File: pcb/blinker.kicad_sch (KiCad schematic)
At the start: 9 parts, among them J1 ISP, U1 ATtiny10-TS

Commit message: Making progress
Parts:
- removed D3: LED, LED_SMD:LED_0603_1608Metric, symbol Device:LED
- removed R1: 220, Resistor_SMD:R_0603_1608Metric, symbol Device:R
- added D10, D11, D12, D13, D2, D3, D4, D5, D6, D7, D8, D9: WS2812B, LED_SMD:LED_Wurth_150044M155260, symbol LED:WS2812B
- added JP2: Jumper_2_Open, Jumper:SolderJumper-2_P1.3mm_Open_TrianglePad1.0x1.5mm, symbol Jumper:Jumper_2_Open
- added U2: M24C01-FDW, Package_SO:TSSOP-8_4.4x3mm_P0.65mm, symbol Memory_EEPROM:M24C01-FDW
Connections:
- net 2.7VCC: now also D10.1 (VDD), D11.1 (VDD), D12.1 (VDD), D13.1 (VDD)
- net 5VCC: now also JP2.2 (B), U2.8 (VCC)
- net GND: now also D2.3 (VSS), D3.3 (VSS), D4.3 (VSS), D5.3 (VSS), U2.1 (E0), U2.2 (E1), U2.3 (E2), U2.4 (VSS)
- net LED renamed LEDSTRING
- net LEDSTRING: now also D2.4 (DIN)
- net TPICLK renamed ROMSCL
- net ROMSCL: now also U2.6 (SCL)
- net TPIDATA renamed ROMSDA
- net ROMSDA: now also U2.5 (SDA)
- new net: D6.1 (VDD), D7.1 (VDD), D8.1 (VDD), D9.1 (VDD)
- new net: D10.4 (DIN), D9.2 (DOUT)
- new net: D6.3 (VSS), D7.3 (VSS), D8.3 (VSS), D9.3 (VSS)
- new net: D8.2 (DOUT), D9.4 (DIN)
- new net: D12.2 (DOUT), D13.4 (DIN)
- new net: D10.3 (VSS), D11.3 (VSS), D12.3 (VSS), D13.3 (VSS)
- new net: D11.2 (DOUT), D12.4 (DIN)
- new net: JP2.1 (A), U2.7 (~{WC})
- new net: D2.1 (VDD), D3.1 (VDD), D4.1 (VDD), D5.1 (VDD)
- new net: D5.2 (DOUT), D6.4 (DIN)
- new net: D4.2 (DOUT), D5.4 (DIN)
- new net: D2.2 (DOUT), D3.4 (DIN)
- new net: D10.2 (DOUT), D11.4 (DIN)
- new net: D7.2 (DOUT), D8.4 (DIN)
- new net: D6.2 (DOUT), D7.4 (DIN)
- new net: D3.2 (DOUT), D4.4 (DIN)

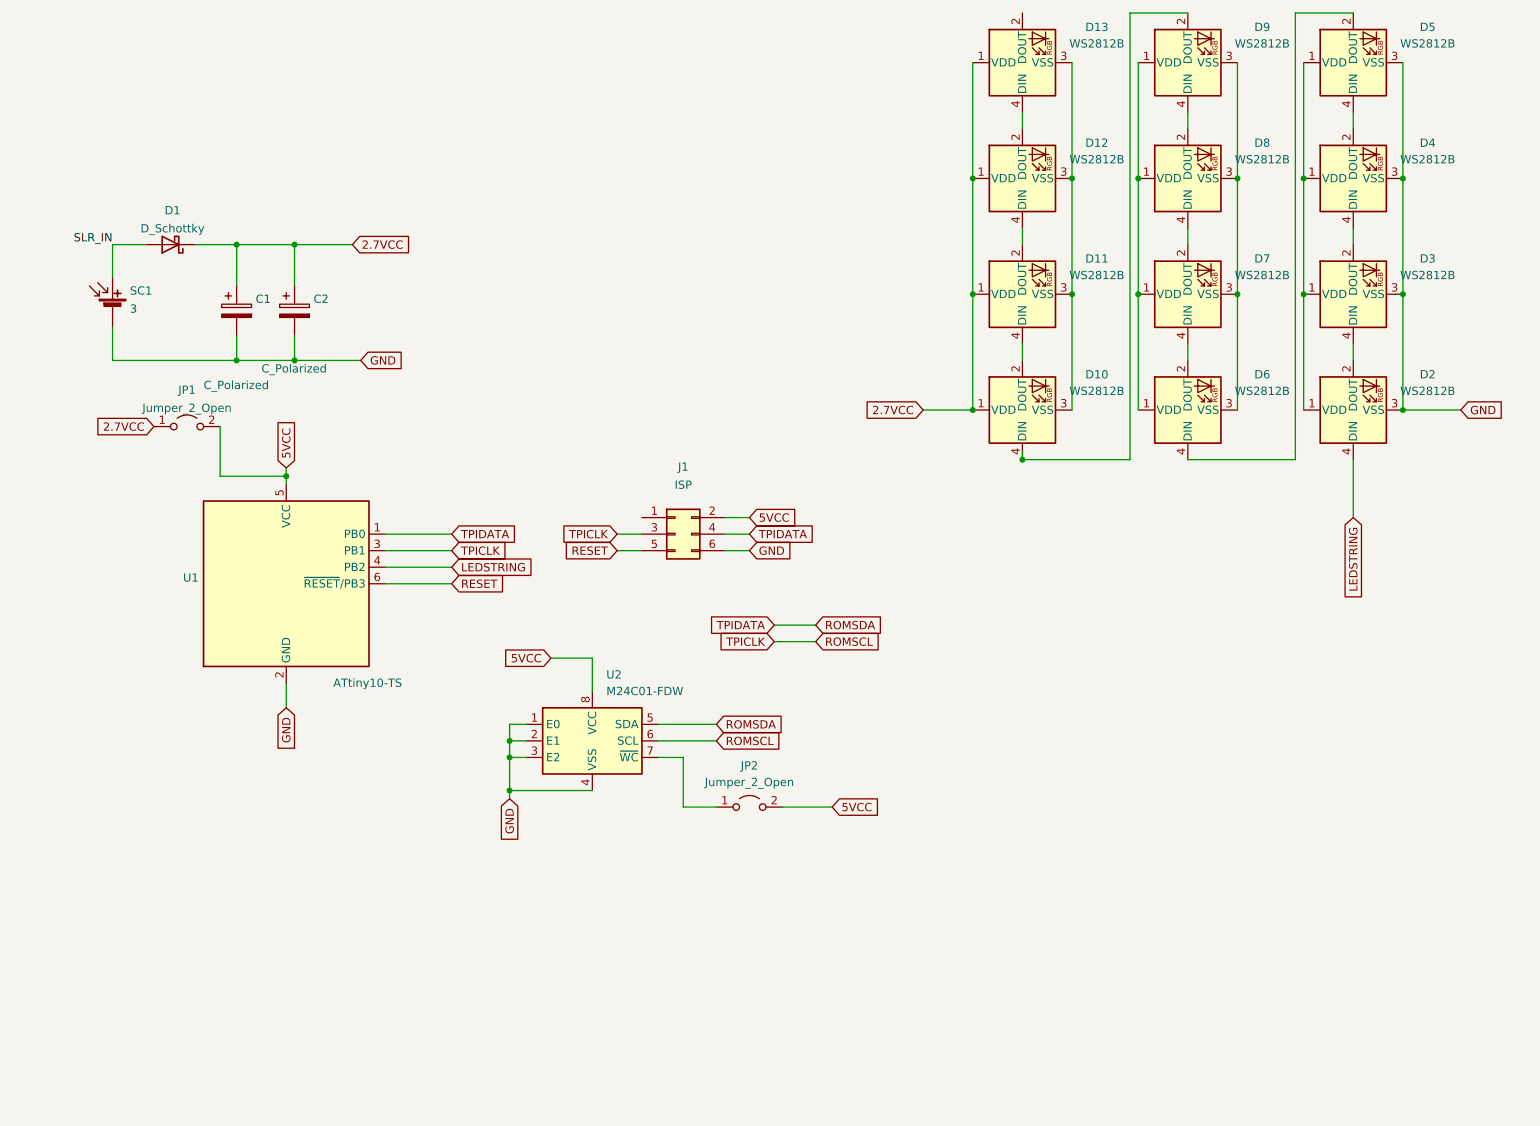
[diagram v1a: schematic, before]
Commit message: Adding decoupling caps and RC filter.
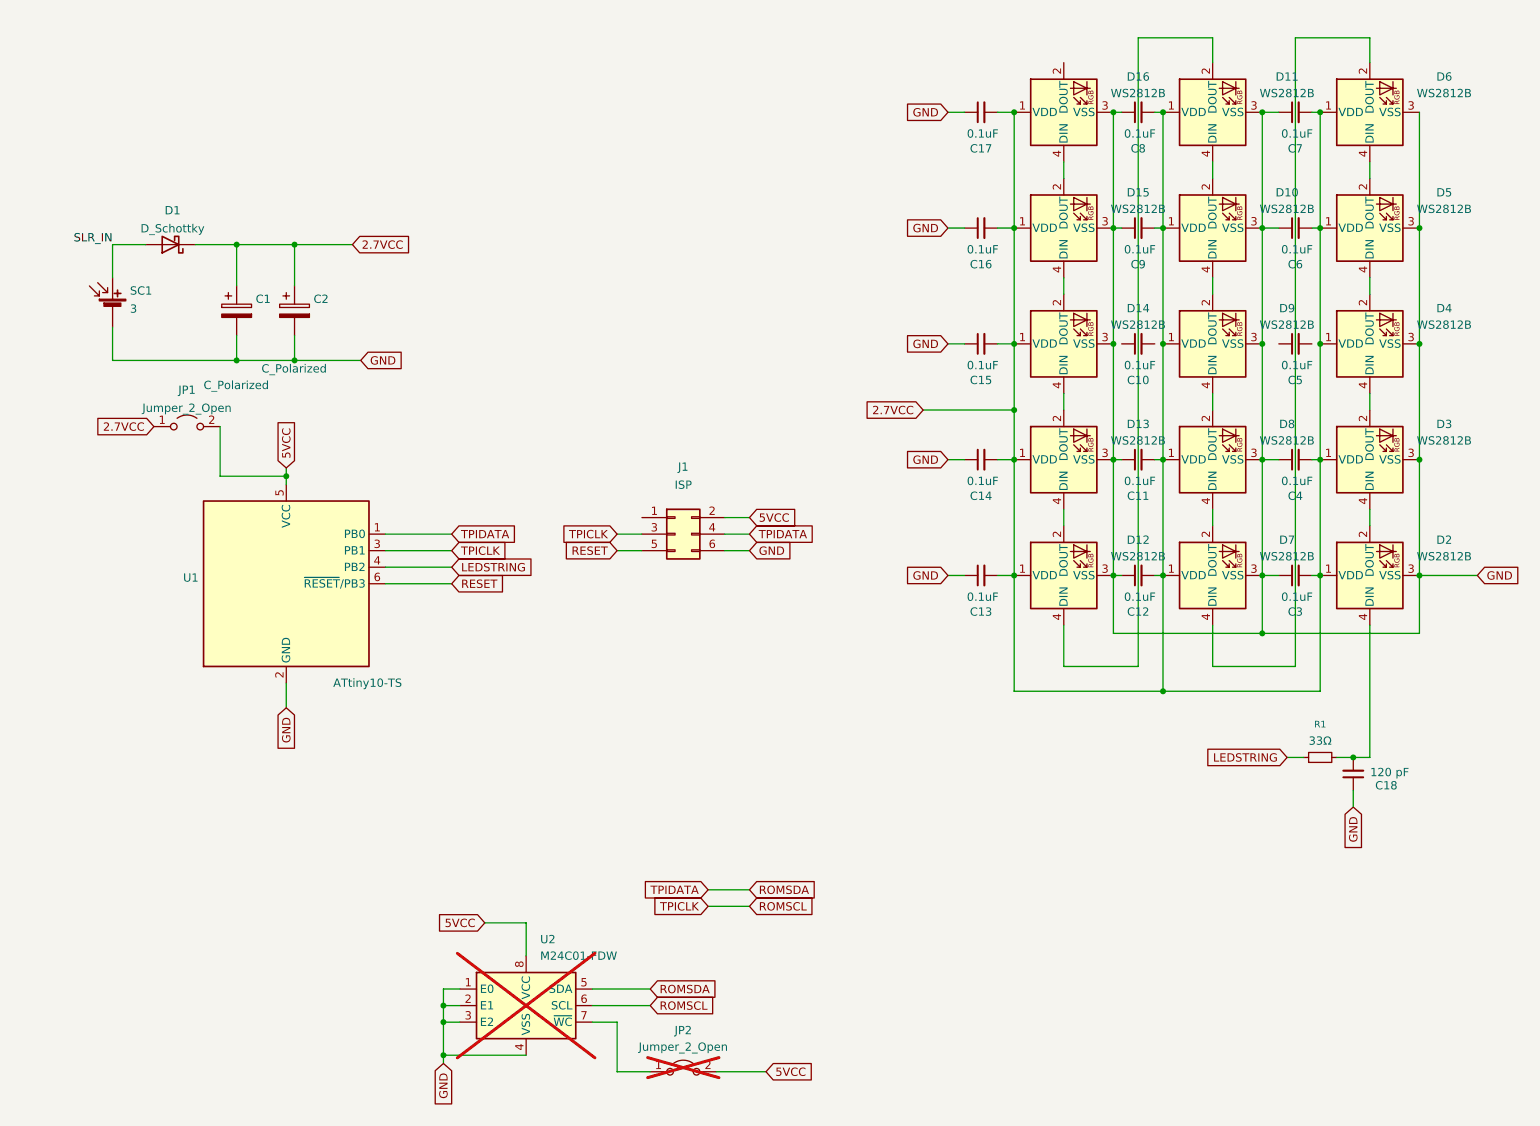
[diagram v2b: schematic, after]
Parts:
- added C10, C11, C12, C13, C14, C15, C16, C17, C3, C4, C5, C6, C7, C8, C9: 0.1uF, Capacitor_SMD:C_01005_0402Metric, symbol Device:C_Small
- added C18: 120 pF, Capacitor_SMD:C_01005_0402Metric, symbol Device:C_Small
- added D14, D15, D16: WS2812B, LED_SMD:LED_Wurth_150044M155260, symbol LED:WS2812B
- added R1: 33Ω, Resistor_SMD:R_0603_1608Metric, symbol Device:R_Small
- JP2, U2: now not fitted; now left out of the parts list
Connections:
- net 2.7VCC: now also D2.1 (VDD), D3.1 (VDD), D4.1 (VDD), D5.1 (VDD), D6.1 (VDD), D7.1 (VDD), D8.1 (VDD), D9.1 (VDD), C11.2, C12.2, C13.2, C14.2, C15.2, C16.2, C17.2, C3.2, C4.2, C6.2, C7.2, C8.2, C9.2, D14.1 (VDD), D15.1 (VDD), D16.1 (VDD)
- net GND: now also D10.3 (VSS), D11.3 (VSS), D12.3 (VSS), D13.3 (VSS), D6.3 (VSS), D7.3 (VSS), D8.3 (VSS), D9.3 (VSS), C11.1, C12.1, C13.1, C14.1, C15.1, C16.1, C17.1, C18.1, C3.1, C4.1, C6.1, C7.1, C8.1, C9.1, D14.3 (VSS), D15.3 (VSS), D16.3 (VSS)
- net LEDSTRING: now also R1.1; no longer D2.4 (DIN)
- net at D13.2 (DOUT): now also D14.4 (DIN)
- new net: D15.2 (DOUT), D16.4 (DIN)
- new net: D14.2 (DOUT), D15.4 (DIN)
- new net: C18.2, D2.4 (DIN), R1.2
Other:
- moved on the sheet: D10, D11, D12, D13, D2, D3, D4, D5, D6, D7, D8, D9

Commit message: Nearly ready to order.
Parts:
- C1, C2, J1, JP1, SC1: now left out of the parts list
- C10, C11, C12, C13, C14, C15, C16, C17, C3, C4, C5, C6, C7, C8, C9: MPN (none) -> 0402YD104KAT2A KYOCERA AVX 0402 100 nF 16 V ±10 % Tolerance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
- C18: MPN (none) -> 04023C121KAT2A KYOCERA AVX Multilayer Ceramic Capacitors ML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
- D1: MPN (none) -> B140WS-7 Diodes Inc. Rectifier Diode, Schottky, 1 Phase, 1 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
- D10, D11, D12, D13, D14, D15, D16, D2, D3, D4, D5, D6, D7, D8, D9: MPN (none) -> LTST-E133CEGBK Lite-On Triple Color LED, Ultra Bright Red/u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
- R1: MPN (none) -> ERJ-PA3F33R0V Panasonic Res Thick Film 0603 33 Ohm 1% 0.25W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
- U1: MPN (none) -> ATTINY10-TSHR Mcu 8-BIT Microchip AVR Risc 1KB Flash 2.5V/3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
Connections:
- net 2.7VCC: now also C10.2, C5.1
- net GND: now also C10.1, C5.2
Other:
- moved on the sheet: C5

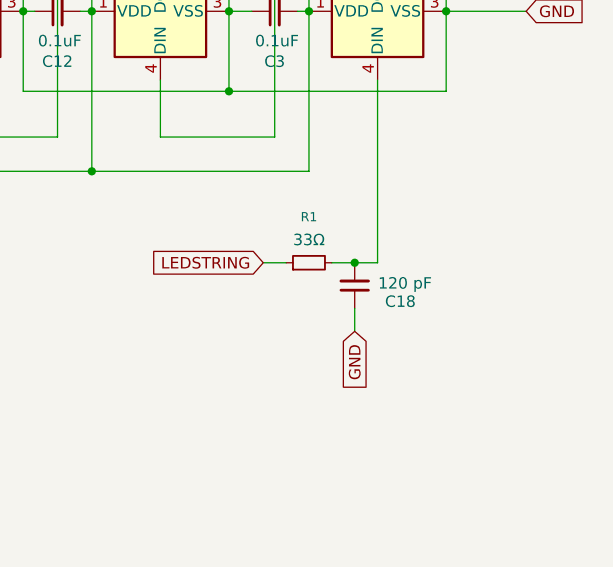
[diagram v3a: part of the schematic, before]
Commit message: Fix 0402 metric vs imperial problem.
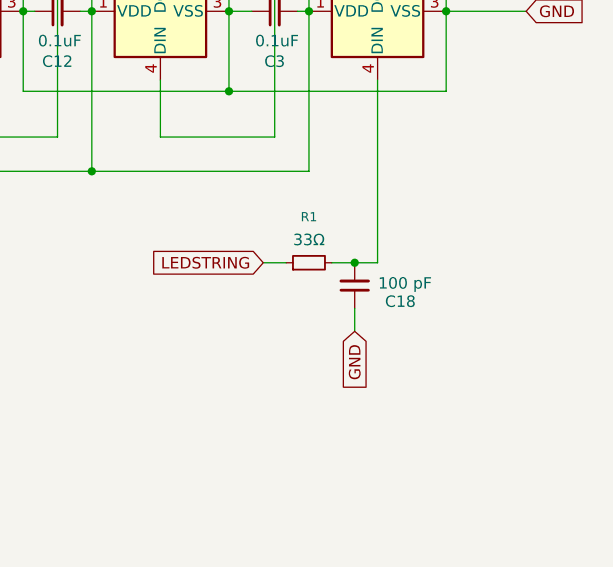
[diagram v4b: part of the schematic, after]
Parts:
- C10, C11, C12, C13, C14, C15, C16, C17, C3, C4, C5, C6, C7, C8, C9: MPN 0402YD104KAT2A KYOCERA AVX 0402 100 nF 16 V ±10 % Tolerance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 -> 01016D104KAT2A KYOCERA AVX 01005 (0402Metric) CERAMIC CAPAC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
- C18: value 120 pF -> 100 pF; MPN 04023C121KAT2A KYOCERA AVX Multilayer Ceramic Capacitors ML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 -> 01016D101KAT2A KYOCERA AVX Capacitor, SMD, MultiLayer Ceram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
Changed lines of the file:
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@@
 	(paper "A4")
 	(title_block
-		(rev "2.0")
+		(rev "2.01")
 	)
 	(junction
@@
 			)
 		)
-		(property "MPN" "0402YD104KAT2A KYOCERA AVX 0402 100 nF 16 V ±10 % Tolerance X5R Surface Mount Multilayer Ceramic Capacitor "
+		(property "MPN" "01016D104KAT2A KYOCERA AVX 01005 (0402Metric) CERAMIC CAPACITOR ceramic capacitor 6.3V 0.1muF ±10% X5R"
 			(at 245.11 95.25 90)
 			(effects
@@
 			)
 		)
-		(property "MPN" "0402YD104KAT2A KYOCERA AVX 0402 100 nF 16 V ±10 % Tolerance X5R Surface Mount Multilayer Ceramic Capacitor "
+		(property "MPN" "01016D104KAT2A KYOCERA AVX 01005 (0402Metric) CERAMIC CAPACITOR ceramic capacitor 6.3V 0.1muF ±10% X5R"
 			(at 220.98 113.03 90)
 			(effects
@@
 			)
 		)
-		(property "MPN" "0402YD104KAT2A KYOCERA AVX 0402 100 nF 16 V ±10 % Tolerance X5R Surface Mount Multilayer Ceramic Capacitor "
+		(property "MPN" "01016D104KAT2A KYOCERA AVX 01005 (0402Metric) CERAMIC CAPACITOR ceramic capacitor 6.3V 0.1muF ±10% X5R"
 			(at 245.11 77.47 90)
 			(effects
@@
 			)
 		)
-		(property "MPN" "0402YD104KAT2A KYOCERA AVX 0402 100 nF 16 V ±10 % Tolerance X5R Surface Mount Multilayer Ceramic Capacitor "
+		(property "MPN" "01016D104KAT2A KYOCERA AVX 01005 (0402Metric) CERAMIC CAPACITOR ceramic capacitor 6.3V 0.1muF ±10% X5R"
 			(at 196.85 41.91 90)
 			(effects
@@
 			)
 		)
-		(property "MPN" "0402YD104KAT2A KYOCERA AVX 0402 100 nF 16 V ±10 % Tolerance X5R Surface Mount Multilayer Ceramic Capacitor "
+		(property "MPN" "01016D104KAT2A KYOCERA AVX 01005 (0402Metric) CERAMIC CAPACITOR ceramic capacitor 6.3V 0.1muF ±10% X5R"
 			(at 220.98 77.47 90)
 			(effects
@@
 			)
 		)
-		(property "MPN" "0402YD104KAT2A KYOCERA AVX 0402 100 nF 16 V ±10 % Tolerance X5R Surface Mount Multilayer Ceramic Capacitor "
+		(property "MPN" "01016D104KAT2A KYOCERA AVX 01005 (0402Metric) CERAMIC CAPACITOR ceramic capacitor 6.3V 0.1muF ±10% X5R"
 			(at 220.98 41.91 90)
 			(effects
@@
 			)
 		)
-		(property "MPN" "0402YD104KAT2A KYOCERA AVX 0402 100 nF 16 V ±10 % Tolerance X5R Surface Mount Multilayer Ceramic Capacitor "
+		(property "MPN" "01016D104KAT2A KYOCERA AVX 01005 (0402Metric) CERAMIC CAPACITOR ceramic capacitor 6.3V 0.1muF ±10% X5R"
 			(at 220.98 95.25 90)
 			(effects
@@
 			)
 		)
-		(property "MPN" "0402YD104KAT2A KYOCERA AVX 0402 100 nF 16 V ±10 % Tolerance X5R Surface Mount Multilayer Ceramic Capacitor "
+		(property "MPN" "01016D104KAT2A KYOCERA AVX 01005 (0402Metric) CERAMIC CAPACITOR ceramic capacitor 6.3V 0.1muF ±10% X5R"
 			(at 220.98 59.69 90)
 			(effects
@@
 			)
 		)
-		(property "MPN" "0402YD104KAT2A KYOCERA AVX 0402 100 nF 16 V ±10 % Tolerance X5R Surface Mount Multilayer Ceramic Capacitor "
+		(property "MPN" "01016D104KAT2A KYOCERA AVX 01005 (0402Metric) CERAMIC CAPACITOR ceramic capacitor 6.3V 0.1muF ±10% X5R"
 			(at 245.11 59.69 90)
 			(effects
@@
 			)
 		)
-		(property "MPN" "0402YD104KAT2A KYOCERA AVX 0402 100 nF 16 V ±10 % Tolerance X5R Surface Mount Multilayer Ceramic Capacitor "
+		(property "MPN" "01016D104KAT2A KYOCERA AVX 01005 (0402Metric) CERAMIC CAPACITOR ceramic capacitor 6.3V 0.1muF ±10% X5R"
 			(at 196.85 59.69 90)
 			(effects
@@
 			)
 		)
-		(property "MPN" "0402YD104KAT2A KYOCERA AVX 0402 100 nF 16 V ±10 % Tolerance X5R Surface Mount Multilayer Ceramic Capacitor "
+		(property "MPN" "01016D104KAT2A KYOCERA AVX 01005 (0402Metric) CERAMIC CAPACITOR ceramic capacitor 6.3V 0.1muF ±10% X5R"
 			(at 196.85 113.03 90)
 			(effects
@@
 			)
 		)
-		(property "MPN" "0402YD104KAT2A KYOCERA AVX 0402 100 nF 16 V ±10 % Tolerance X5R Surface Mount Multilayer Ceramic Capacitor "
+		(property "MPN" "01016D104KAT2A KYOCERA AVX 01005 (0402Metric) CERAMIC CAPACITOR ceramic capacitor 6.3V 0.1muF ±10% X5R"
 			(at 245.11 113.03 90)
 			(effects
@@
 			)
 		)
-		(property "Value" "120 pF"
+		(property "Value" "100 pF"
 			(at 259.588 143.256 0)
 			(effects
@@
 			)
 		)
-		(property "MPN" "04023C121KAT2A KYOCERA AVX Multilayer Ceramic Capacitors MLCC - SMD/SMT 25V 120pF X7R 0402 10%"
+		(property "MPN" "01016D101KAT2A KYOCERA AVX Capacitor, SMD, MultiLayer Ceramic (MLCC), 01005 Case, 6.3Vdc, X5R, 100pF, ±10%, ø7T/R"
 			(at 254 143.51 0)
 			(effects
@@
 			)
 		)
-		(property "MPN" "0402YD104KAT2A KYOCERA AVX 0402 100 nF 16 V ±10 % Tolerance X5R Surface Mount Multilayer Ceramic Capacitor "
+		(property "MPN" "01016D104KAT2A KYOCERA AVX 01005 (0402Metric) CERAMIC CAPACITOR ceramic capacitor 6.3V 0.1muF ±10% X5R"
 			(at 245.11 41.91 90)
 			(effects
@@
 			)
 		)
-		(property "MPN" "0402YD104KAT2A KYOCERA AVX 0402 100 nF 16 V ±10 % Tolerance X5R Surface Mount Multilayer Ceramic Capacitor "
+		(property "MPN" "01016D104KAT2A KYOCERA AVX 01005 (0402Metric) CERAMIC CAPACITOR ceramic capacitor 6.3V 0.1muF ±10% X5R"
 			(at 196.85 77.47 90)
 			(effects
@@
 			)
 		)
-		(property "MPN" "0402YD104KAT2A KYOCERA AVX 0402 100 nF 16 V ±10 % Tolerance X5R Surface Mount Multilayer Ceramic Capacitor "
+		(property "MPN" "01016D104KAT2A KYOCERA AVX 01005 (0402Metric) CERAMIC CAPACITOR ceramic capacitor 6.3V 0.1muF ±10% X5R"
 			(at 196.85 95.25 90)
 			(effects
